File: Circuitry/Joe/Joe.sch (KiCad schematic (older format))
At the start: 16 parts, among them U1 DS3231M

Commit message: sch review changes, eeprom, linear image sensor.
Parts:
- removed C?: C_Small, symbol Device:C_Small
- removed C?: CP_Small, symbol Device:CP_Small
- removed R? (x4): R, symbol Device:R
- removed U1: DS3231M, Package_SO:SOIC-16W_7.5x10.3mm_P1.27mm, symbol Timer_RTC:DS3231M
- added C?: 0.1uF, symbol Device:CP_Small
- added C?: 0.1uF, symbol Device:C_Small
- added C? (x2): 1uF, symbol Device:C
- added J?: Screw_Terminal_01x09, symbol Connector:Screw_Terminal_01x09
- added Q? (x4): 2N7000, Package_TO_SOT_THT:TO-92_Inline, symbol Transistor_FET:2N7000
- added R? (x12): 10k, symbol Device:R
- added R? (x4): R, symbol Device:R
- added U?: DS3231M, Package_SO:SOIC-16W_7.5x10.3mm_P1.27mm, symbol Timer_RTC:DS3231M
- added U? (x4): GL5528, symbol Custom:GL5528
- added U?: UFDFPN8-MC, symbol Custom:UFDFPN8-MC
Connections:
- net labels added: +3V3, 1HZ, AI1, AI2, AI3, AI4, AI5, AI6, CRYSTAL2, DI1, DI2, PHO1, PHO2, PHO3, PHO4, SCL, SCL2, SDA2, SQW2, ST, STBY, TEMP, TMR_RST, VID
- net labels removed: 3.3V, 5V, PHOV, TEMPV
- wire segments 54 -> 131
- no-connect marks 1 -> 2
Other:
- note added: "JOE LOFTUS"
- note added: "Photocells"
- moved on the sheet: D?, J?, R?

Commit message: Fixed symbol libraries
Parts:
- U?: symbol Custom:DF12-20DS -> Joe-rescue:DF12-20DS-Custom
- U? (x4): symbol Custom:GL5528 -> Joe-rescue:GL5528-Custom
- U?: symbol Custom:UFDFPN8-MC -> Joe-rescue:UFDFPN8-MC-Custom
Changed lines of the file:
@@
 Microcontroller
 $Comp
-L Custom:DF12-20DS U?
+L Joe-rescue:DF12-20DS-Custom U?
 U 1 1 5D1584F8
 P 6000 1450
@@
 $EndComp
 $Comp
-L Custom:GL5528 U?
+L Joe-rescue:GL5528-Custom U?
 U 1 1 5D1D3A1F
 P 1700 3525
@@
 	2150 3525 2150 3300
 $Comp
-L Custom:GL5528 U?
+L Joe-rescue:GL5528-Custom U?
 U 1 1 5D22238E
 P 1725 4650
@@
 	2175 4650 2175 4425
 $Comp
-L Custom:GL5528 U?
+L Joe-rescue:GL5528-Custom U?
 U 1 1 5D224EEE
 P 1750 5800
@@
 	2200 5800 2200 5575
 $Comp
-L Custom:GL5528 U?
+L Joe-rescue:GL5528-Custom U?
 U 1 1 5D229453
 P 1775 6950
@@
 ST
 $Comp
-L Custom:UFDFPN8-MC U?
+L Joe-rescue:UFDFPN8-MC-Custom U?
 U 1 1 5D2D63AB
 P 7450 4400

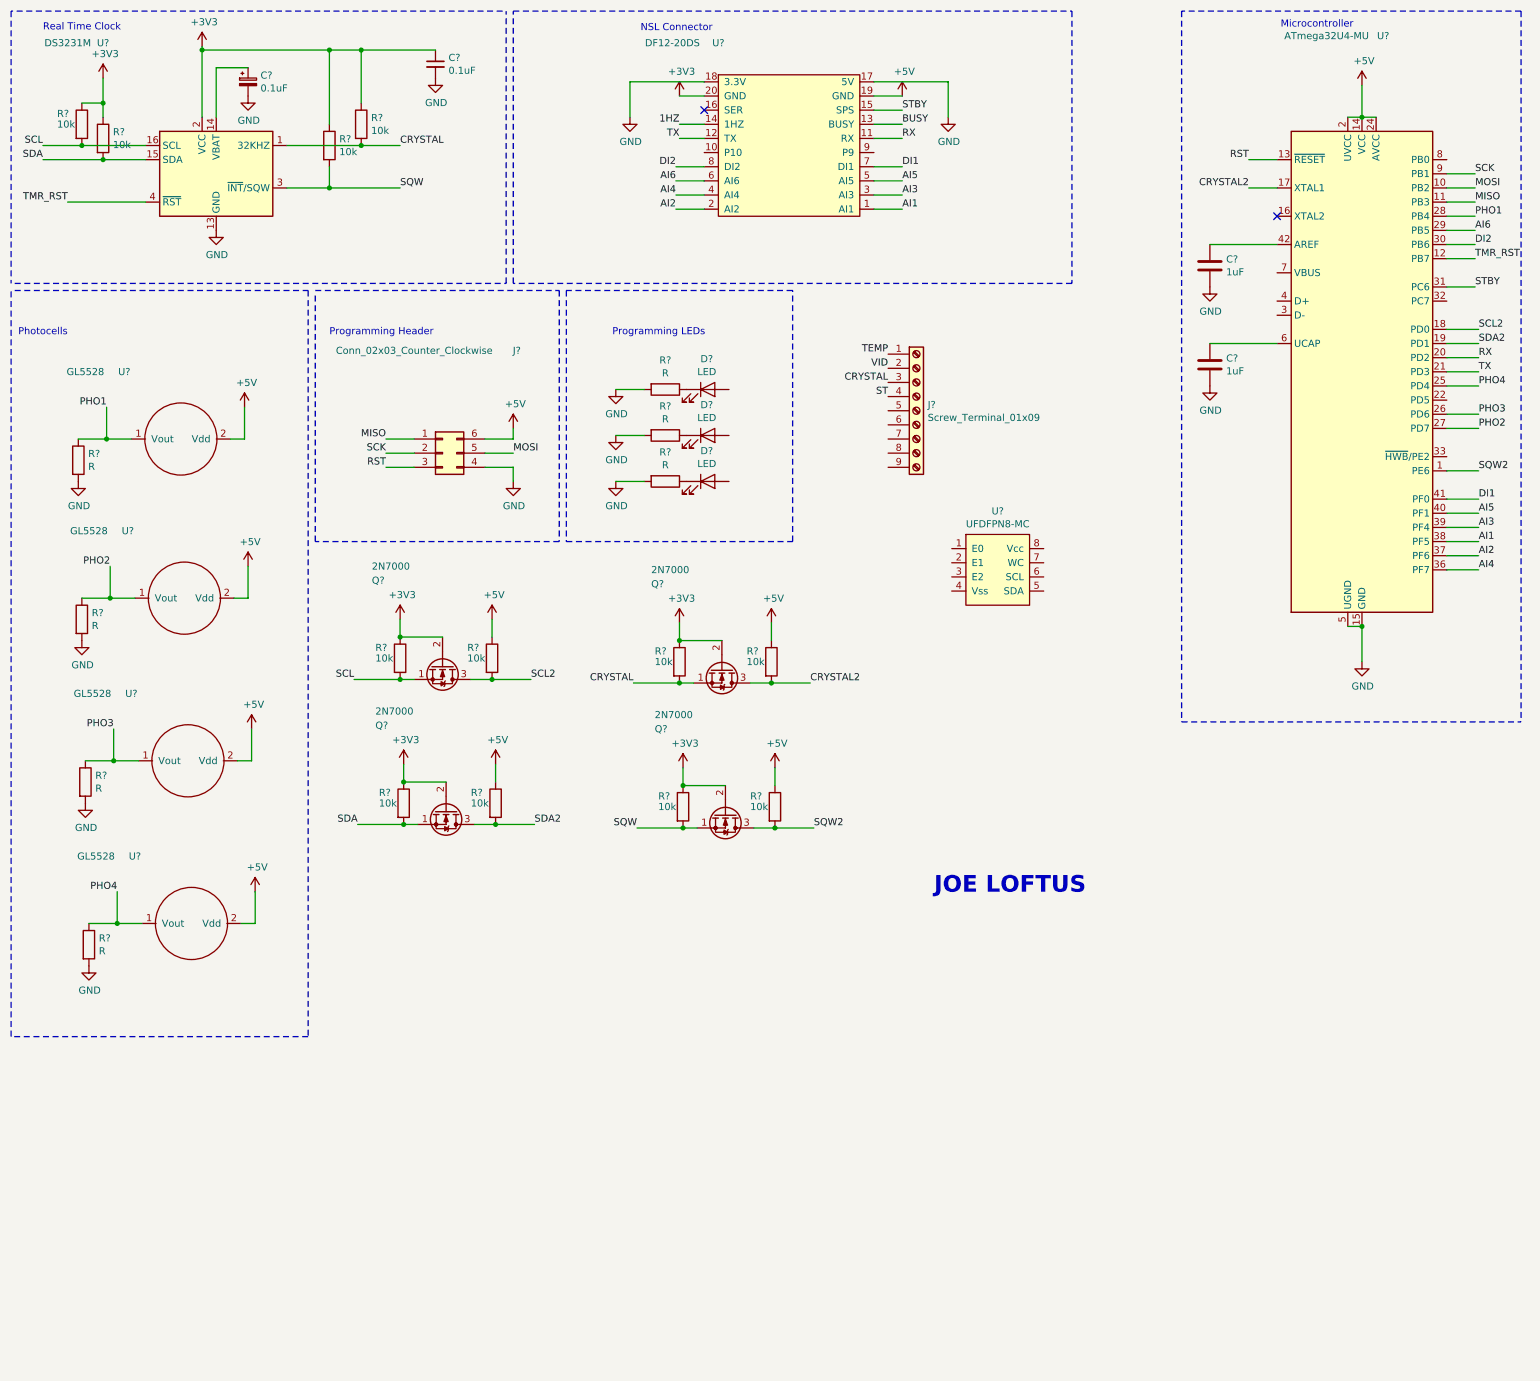
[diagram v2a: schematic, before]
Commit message: changes to Joe: part lables, BW, and shift regs
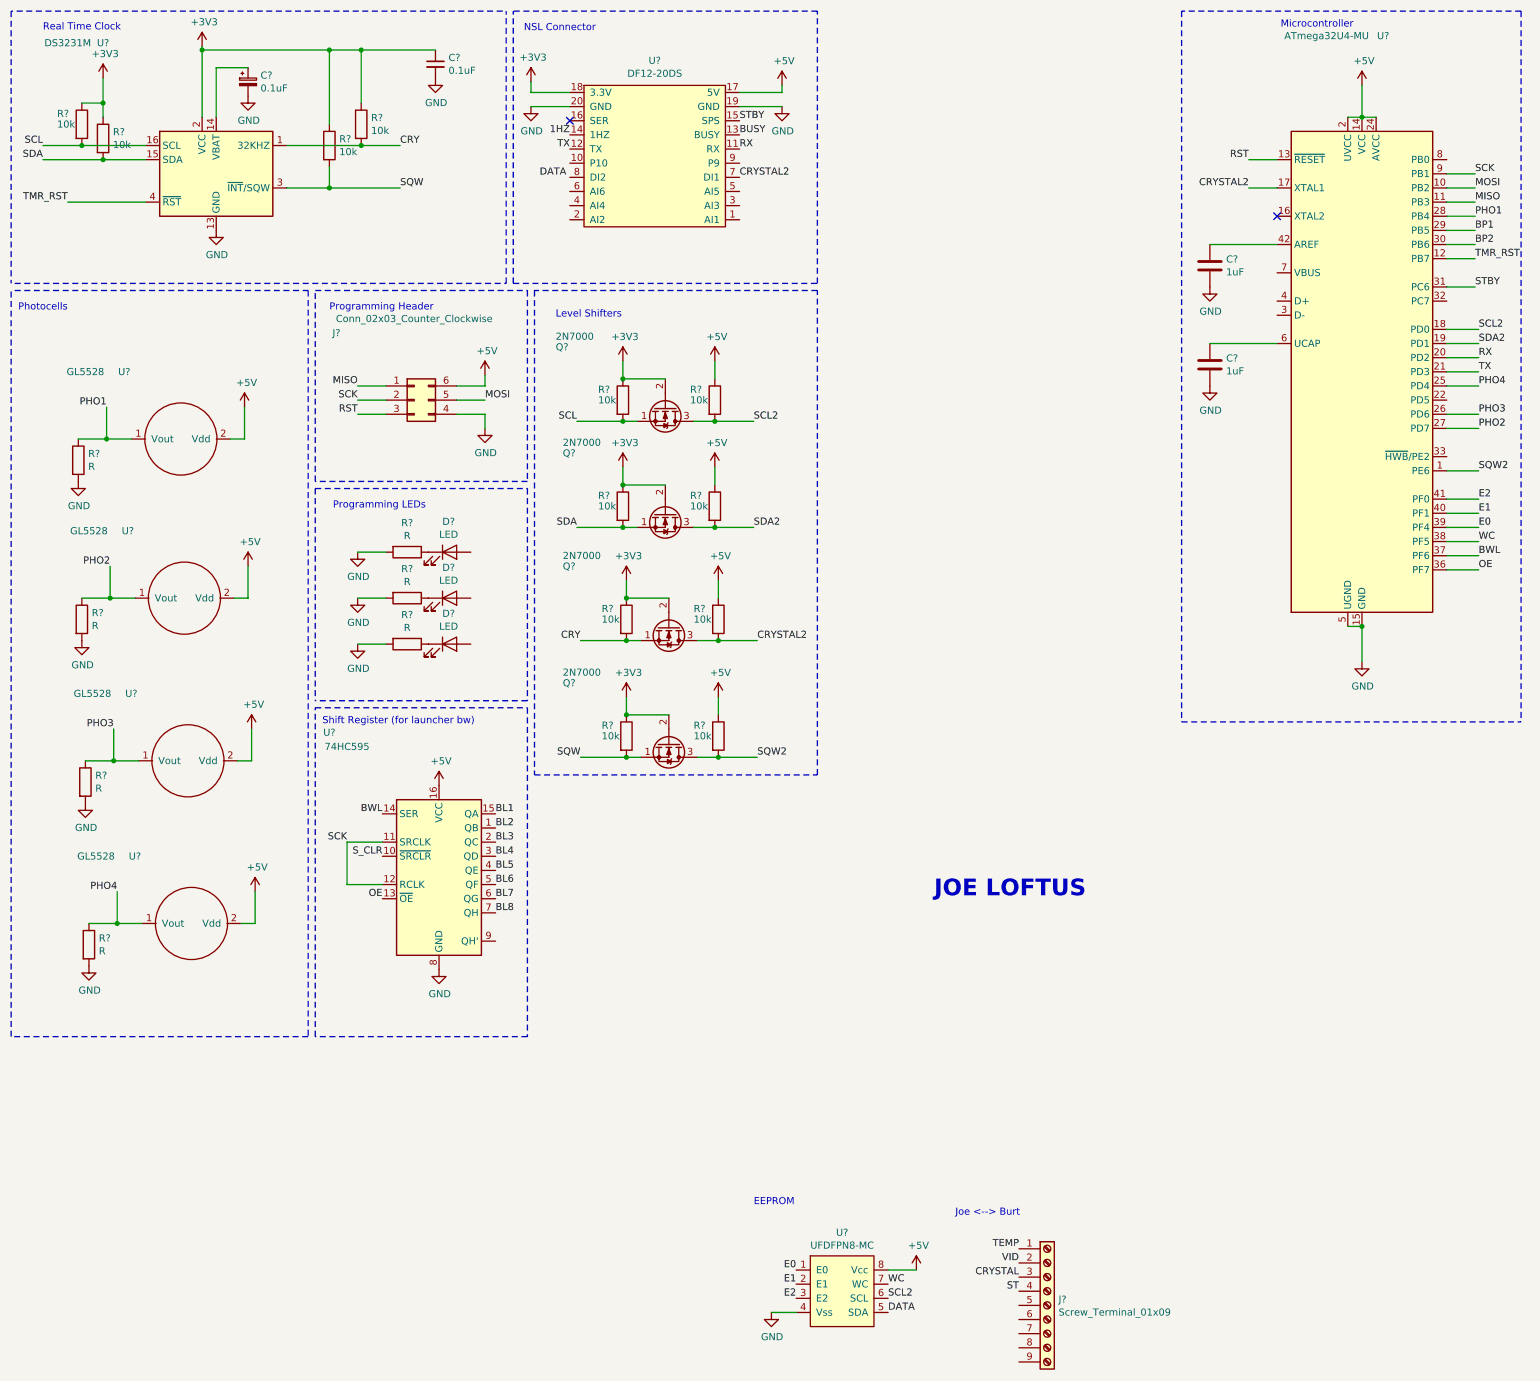
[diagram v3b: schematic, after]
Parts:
- removed U?: DF12-20DS, symbol Joe-rescue:DF12-20DS-Custom
- added U?: 74HC595, symbol 74xx:74HC595
- added U?: DF12-20DS, symbol Custom:DF12-20DS
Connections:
- net AI1 is gone; now on net WC: U?.38 (PF5)
- net AI3 is gone; now on net E0: U?.39 (PF4)
- net AI5 is gone; now on net E1: U?.40 (PF1)
- net DI1 is gone; now on net E2: U?.41 (PF0)
- net +3V3: now also U?.18 (3.3V)
- net +5V: now also U?.8 (Vcc), U?.16 (VCC), U?.17 (5V)
- net 1HZ: now also U?.14 (1HZ)
- net BUSY: now also U?.13 (BUSY)
- net CRYSTAL: no longer Q?.1 (S), R?.2, R?.2, U?.1 (32KHZ)
- net CRYSTAL2: now also U?.7 (DI1)
- net GND: now also U?.4 (Vss), U?.19 (GND), U?.20 (GND), U?.8 (GND)
- net RX: now also U?.11 (RX)
- net SCK: now also U?.11 (SRCLK), U?.12 (RCLK)
- net SCL2: now also U?.6 (SCL)
- net STBY: now also U?.15 (SPS)
- net TX: now also U?.12 (TX)
- net E0: now reaches U?.1 (E0)
- net E1: now reaches U?.2 (E1)
- net E2: now reaches U?.3 (E2)
- net DATA: now reaches U?.5 (SDA)
- net WC: now reaches U?.7 (WC)
- net AI2 renamed BWL
- net BWL: now also U?.14 (SER)
- net AI4 renamed OE
- net OE: now also U?.13 (~OE)
- net AI6 renamed BP1
- net DI2 renamed BP2
- new net BL1: U?.15 (QA)
- new net BL2: U?.1 (QB)
- new net BL3: U?.2 (QC)
- new net BL4: U?.3 (QD)
- new net BL5: U?.4 (QE)
- new net BL6: U?.5 (QF)
- new net BL7: U?.6 (QG)
- new net BL8: U?.7 (QH)
- new net CRY: Q?.1 (S), R?.2, R?.2, U?.1 (32KHZ)
- new net S_CLR: U?.10 (~SRCLR)
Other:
- note added: "EEPROM\n"
- note added: "Joe <--> Burt\n"
- note added: "Level Shifters"
- note added: "Shift Register (for launcher bw)"
- moved on the sheet: D?, J?, Q?, R?, U?

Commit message: screw terminal on joe
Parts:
- removed J?: Screw_Terminal_01x09, symbol Connector:Screw_Terminal_01x09
- added J?: Screw_Terminal_01x10, symbol Connector:Screw_Terminal_01x10
- added J?: Screw_Terminal_01x06, symbol Connector:Screw_Terminal_01x06
- U?: symbol Custom:DF12-20DS -> Joe-rescue:DF12-20DS-Custom
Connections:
- net BL1: now also J?.1 (Pin_1)
- net BL2: now also J?.2 (Pin_2)
- net BL3: now also J?.3 (Pin_3)
- net BL4: now also J?.4 (Pin_4)
- net BL5: now also J?.5 (Pin_5)
- net BL6: now also J?.6 (Pin_6)
- net BL7: now also J?.7 (Pin_7)
- net BL8: now also J?.8 (Pin_8)
- net BP1: now also J?.5 (Pin_5)
- net BP2: now also J?.6 (Pin_6)
- net CRYSTAL: now also J?.3 (Pin_3)
- net ST: now also J?.4 (Pin_4)
- net TEMP: now also J?.1 (Pin_1)
- net VID: now also J?.2 (Pin_2)
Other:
- moved on the sheet: U?
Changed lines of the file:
@@
 Text Label 10875 3150 0    50   ~ 0
 PHO4
-Text Label 7625 9250 2    50   ~ 0
+Text Label 6950 4875 2    50   ~ 0
 TEMP
-Text Label 7625 9450 2    50   ~ 0
+Text Label 6950 5075 2    50   ~ 0
 CRYSTAL
 $Comp
@@
 Wire Wire Line
 	10650 2450 10850 2450
-$Comp
-L Connector:Screw_Terminal_01x09 J?
-U 1 1 5D265C96
-P 7825 9650
-F 0 "J?" H 7905 9692 50  0000 L CNN
-F 1 "Screw_Terminal_01x09" H 7905 9601 50  0000 L CNN
-F 2 "" H 7825 9650 50  0001 C CNN
-F 3 "~" H 7825 9650 50  0001 C CNN
-	1    7825 9650
-	1    0    0    -1
-$EndComp
-Text Label 7625 9350 2    50   ~ 0
+Text Label 6950 4975 2    50   ~ 0
 VID
-Text Label 7625 9550 2    50   ~ 0
+Text Label 6950 5175 2    50   ~ 0
 ST
 $Comp
 L Joe-rescue:UFDFPN8-MC-Custom U?
 U 1 1 5D2D63AB
-P 6350 9500
-F 0 "U?" H 6375 9865 50  0000 C CNN
-F 1 "UFDFPN8-MC" H 6375 9774 50  0000 C CNN
-F 2 "" H 6350 9500 50  0001 C CNN
-F 3 "https://www.st.com/content/ccc/resource/technical/document/datasheet/80/4e/8c/54/f2/63/4c/4a/CD00001012.pdf/files/CD00001012.pdf/jcr:content/translations/en.CD00001012.pdf" H 6350 9500 50  0001 C CNN
-	1    6350 9500
-	1    0    0    -1
-$EndComp
-Text Label 6050 9400 2    50   ~ 0
+P 4925 6900
+F 0 "U?" H 4950 7265 50  0000 C CNN
+F 1 "UFDFPN8-MC" H 4950 7174 50  0000 C CNN
+F 2 "" H 4925 6900 50  0001 C CNN
+F 3 "https://www.st.com/content/ccc/resource/technical/document/datasheet/80/4e/8c/54/f2/63/4c/4a/CD00001012.pdf/files/CD00001012.pdf/jcr:content/translations/en.CD00001012.pdf" H 4925 6900 50  0001 C CNN
+	1    4925 6900
+	1    0    0    -1
+$EndComp
+Text Label 4625 6800 2    50   ~ 0
 E0
-Text Label 6050 9500 2    50   ~ 0
+Text Label 4625 6900 2    50   ~ 0
 E1
-Text Label 6050 9600 2    50   ~ 0
+Text Label 4625 7000 2    50   ~ 0
 E2
 Text Label 10875 4150 0    50   ~ 0
@@
 L power:+5V #PWR?
 U 1 1 5D2B1691
-P 6900 9400
-F 0 "#PWR?" H 6900 9250 50  0001 C CNN
-F 1 "+5V" H 6915 9573 50  0000 C CNN
-F 2 "" H 6900 9400 50  0001 C CNN
-F 3 "" H 6900 9400 50  0001 C CNN
-	1    6900 9400
-	1    0    0    -1
-$EndComp
-Wire Wire Line
-	6700 9400 6900 9400
-Text Label 6700 9500 0    50   ~ 0
+P 5475 6800
+F 0 "#PWR?" H 5475 6650 50  0001 C CNN
+F 1 "+5V" H 5490 6973 50  0000 C CNN
+F 2 "" H 5475 6800 50  0001 C CNN
+F 3 "" H 5475 6800 50  0001 C CNN
+	1    5475 6800
+	1    0    0    -1
+$EndComp
+Wire Wire Line
+	5275 6800 5475 6800
+Text Label 5275 6900 0    50   ~ 0
 WC
-Text Label 6700 9600 0    50   ~ 0
+Text Label 5275 7000 0    50   ~ 0
 SCL2
-Text Label 6700 9700 0    50   ~ 0
+Text Label 5275 7100 0    50   ~ 0
 DATA
 $Comp
 L power:GND #PWR?
 U 1 1 5D2C2E70
-P 5875 9700
-F 0 "#PWR?" H 5875 9450 50  0001 C CNN
-F 1 "GND" H 5880 9527 50  0000 C CNN
-F 2 "" H 5875 9700 50  0001 C CNN
-F 3 "" H 5875 9700 50  0001 C CNN
-	1    5875 9700
-	1    0    0    -1
-$EndComp
-Wire Wire Line
-	6050 9700 5875 9700
+P 4450 7100
+F 0 "#PWR?" H 4450 6850 50  0001 C CNN
+F 1 "GND" H 4455 6927 50  0000 C CNN
+F 2 "" H 4450 7100 50  0001 C CNN
+F 3 "" H 4450 7100 50  0001 C CNN
+	1    4450 7100
+	1    0    0    -1
+$EndComp
+Wire Wire Line
+	4625 7100 4450 7100
 Text Label 10875 4250 0    50   ~ 0
 WC
@@
 Wire Notes Line
 	2650 3825 2650 2475
-Text Notes 5750 8950 0    50   ~ 0
+Text Notes 4325 6350 0    50   ~ 0
 EEPROM\n
 Text Label 4425 1675 2    50   ~ 0
@@
 	1    0    0    -1
 $EndComp
-Text Notes 7175 9025 0    50   ~ 0
+Text Notes 6775 4425 0    50   ~ 0
 Joe <--> Burt\n
 $Comp
@@
 $EndComp
 $Comp
-L Custom:DF12-20DS U?
+L Joe-rescue:DF12-20DS-Custom U?
 U 1 1 5D782D20
 P 5050 1525
@@
 Wire Notes Line
 	6200 5900 6200 2475
+$Comp
+L Connector:Screw_Terminal_01x10 J?
+U 1 1 5D29FE3C
+P 7950 4900
+F 0 "J?" V 8175 4350 50  0000 L CNN
+F 1 "Screw_Terminal_01x10" V 8075 4350 50  0000 L CNN
+F 2 "" H 7950 4900 50  0001 C CNN
+F 3 "~" H 7950 4900 50  0001 C CNN
+	1    7950 4900
+	1    0    0    -1
+$EndComp
+$Comp
+L Connector:Screw_Terminal_01x06 J?
+U 1 1 5D2A1839
+P 7150 5075
+F 0 "J?" V 7375 4725 50  0000 L CNN
+F 1 "Screw_Terminal_01x06" V 7275 4725 50  0000 L CNN
+F 2 "" H 7150 5075 50  0001 C CNN
+F 3 "~" H 7150 5075 50  0001 C CNN
+	1    7150 5075
+	1    0    0    -1
+$EndComp
+Text Label 7750 4500 2    50   ~ 0
+BL1
+Text Label 7750 4600 2    50   ~ 0
+BL2
+Text Label 7750 4700 2    50   ~ 0
+BL3
+Text Label 7750 4800 2    50   ~ 0
+BL4
+Text Label 7750 4900 2    50   ~ 0
+BL5
+Text Label 7750 5000 2    50   ~ 0
+BL6
+Text Label 7750 5100 2    50   ~ 0
+BL7
+Text Label 7750 5200 2    50   ~ 0
+BL8
+Text Label 6950 5275 2    50   ~ 0
+BP1
+Text Label 6950 5375 2    50   ~ 0
+BP2
 $EndSCHEMATC
